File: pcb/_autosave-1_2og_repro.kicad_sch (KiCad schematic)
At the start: 217 parts, among them J1 Pico EzMate, J2 USB_B_Mini, J3 Raw Header, J4 JST PH S3B, J5 Foam, SW1 MX_SW_solder, SW10 MX_SW_solder, SW11 MX_SW_solder, SW12 MX_SW_solder, SW13 MX_SW_solder, SW14 MX_SW_solder, SW15 MX_SW_solder, SW16 MX_SW_solder, SW17 MX_SW_solder, SW18 MX_SW_solder, SW19 MX_SW_solder, SW2 MX_SW_solder, SW20 MX_SW_solder, SW21 MX_SW_solder, SW22 MX_SW_solder, SW23 MX_SW_solder, SW24 MX_SW_solder, SW25 MX_SW_solder, SW26 MX_SW_solder, SW27 MX_SW_solder, SW28 MX_SW_solder, SW29 MX_SW_solder, SW3 MX_SW_solder, SW30 MX_SW_solder, SW31 MX_SW_solder, SW32 MX_SW_solder, SW33 MX_SW_solder, SW34 MX_SW_solder, SW35 MX_SW_solder, SW36 MX_SW_solder, SW37 MX_SW_solder, SW38 MX_SW_solder, SW39 MX_SW_solder, SW4 MX_SW_solder, SW40 MX_SW_solder, SW41 MX_SW_solder, SW42 MX_SW_solder, SW43 MX_SW_solder, SW44 MX_SW_solder, SW45 MX_SW_solder, SW46 MX_SW_solder, SW47 MX_SW_solder, SW48 MX_SW_solder, SW49 MX_SW_solder, SW5 MX_SW_solder, SW50 MX_SW_solder, SW51 MX_SW_solder, SW52 MX_SW_solder, SW53 MX_SW_solder, SW54 MX_SW_solder, SW55 MX_SW_solder, SW56 MX_SW_solder, SW57 MX_SW_solder, SW58 MX_SW_solder, SW59 MX_SW_solder, SW6 MX_SW_solder, SW60 MX_SW_solder, SW61 MX_SW_solder, SW62 MX_SW_solder, SW63 MX_SW_solder, SW64 MX_SW_solder, SW65 MX_SW_solder, SW66 MX_SW_solder, SW67 MX_SW_solder, SW68 MX_SW_solder, SW69 MX_SW_solder, SW7 MX_SW_solder, SW70 MX_SW_solder, SW71 MX_SW_solder, SW72 MX_SW_solder, SW73 MX_SW_solder, SW74 MX_SW_solder, SW75 MX_SW_solder, SW76 MX_SW_solder, SW77 MX_SW_solder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

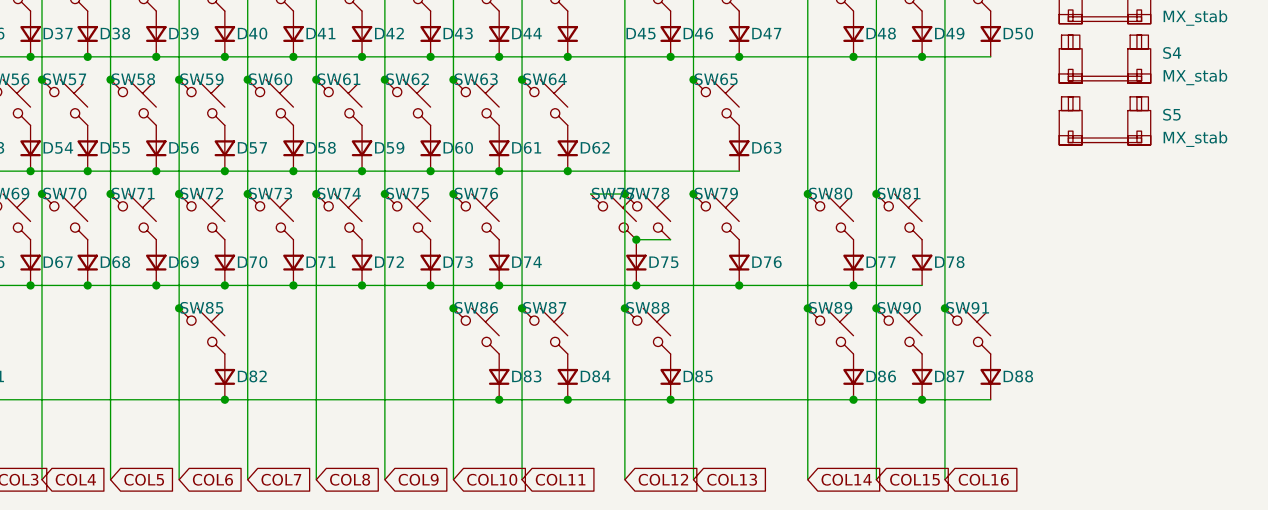
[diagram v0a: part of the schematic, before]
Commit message: add 6u support (firmware does not reflect this yet), usb 0548190519
previous USB is annoying to hand-solder without wick, using through-hole
pins may be less of a pain. 6u support is added because I miss my HHKB.
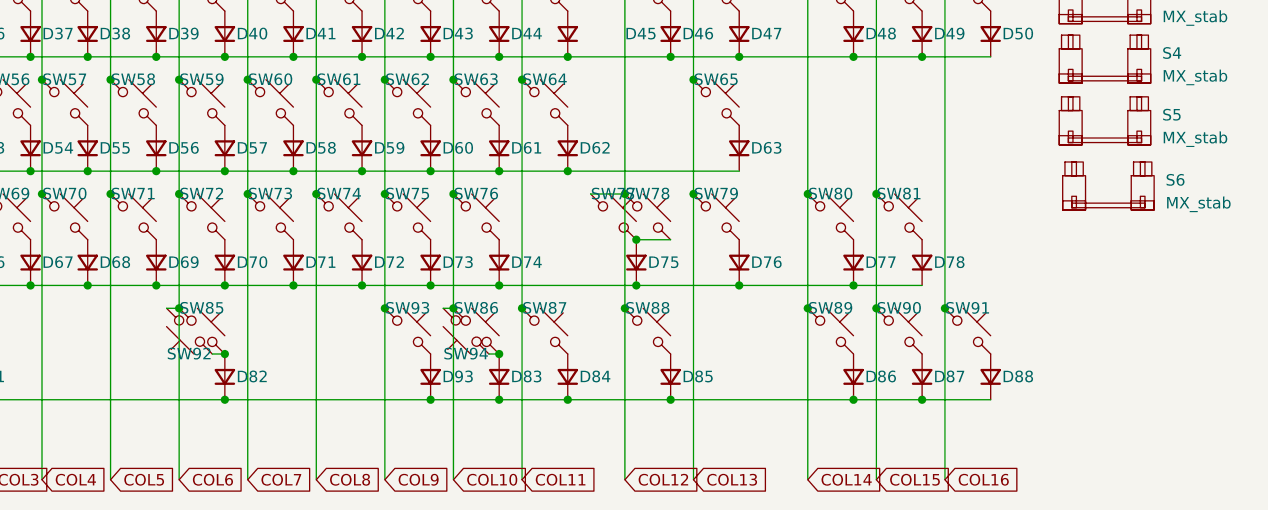
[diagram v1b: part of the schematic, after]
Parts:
- added D93: D_Small, Diode_SMD:D_SOD-123, symbol Device:D_Small
- added S6: MX_stab, marbastlib-mx:STAB_MX_6u, symbol marbastlib-mx:MX_stab
- added SW92, SW94: MX_SW_solder, marbastlib-mx:SW_MX_1u, symbol marbastlib-mx:MX_SW_solder
- added SW93: MX_SW_solder, marbastlib-mx:SW_MX_1.5u, symbol marbastlib-mx:MX_SW_solder
- J2: footprint random-keyboard-parts:Molex-0548190589 -> random-keyboard-parts:Molex-0548190519
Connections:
- net COL10: now also SW94.2
- net COL6: now also SW92.2
- net COL9: now also SW93.1
- net ROW5: now also D93.1 (K)
- net at D82.2 (A), SW85.2: now also SW92.1
- net at D83.2 (A), SW86.2: now also SW94.1
- new net: D93.2 (A), SW93.2
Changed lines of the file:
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@@
   (junction (at 226.06 119.253) (diameter 0) (color 0 0 0 0)
   )
+  (junction (at 191.77 144.653) (diameter 0) (color 0 0 0 0)
+  )
   (junction (at 137.16 154.813) (diameter 0) (color 0 0 0 0)
   )
+  (junction (at 173.99 149.733) (diameter 0) (color 0 0 0 0)
+  )
   (junction (at 139.7 106.553) (diameter 0) (color 0 0 0 0)
   )
@@
   (junction (at 129.54 116.713) (diameter 0) (color 0 0 0 0)
   )
+  (junction (at 204.47 149.733) (diameter 0) (color 0 0 0 0)
+  )
   (junction (at 176.53 106.553) (diameter 0) (color 0 0 0 0)
   )
@@
   (junction (at 133.985 50.165) (diameter 0) (color 0 0 0 0)
   )
+  (junction (at 196.85 154.813) (diameter 0) (color 0 0 0 0)
+  )
   (junction (at 231.14 142.113) (diameter 0) (color 0 0 0 0)
   )
@@
     (stroke (width 0) (type default))
   )
+  (wire (pts (xy 203.327 149.733) (xy 204.47 149.733))
+    (stroke (width 0) (type default))
+  )
   (wire (pts (xy 173.99 104.013) (xy 181.61 104.013))
     (stroke (width 0) (type default))
@@
     (stroke (width 0) (type default))
   )
+  (wire (pts (xy 167.513 144.653) (xy 168.91 144.653))
+    (stroke (width 0) (type default))
+  )
   (polyline (pts (xy 156.845 12.065) (xy 156.845 29.845))
     (stroke (width 0) (type default))
@@
     (stroke (width 0) (type default))
   )
-  (wire (pts (xy 204.47 154.813) (xy 173.99 154.813))
+  (wire (pts (xy 204.47 154.813) (xy 196.85 154.813))
     (stroke (width 0) (type default))
   )
@@
     (stroke (width 0) (type default))
   )
+  (wire (pts (xy 191.77 144.653) (xy 191.77 163.703))
+    (stroke (width 0) (type default))
+  )
   (wire (pts (xy 124.46 131.953) (xy 124.46 144.653))
     (stroke (width 0) (type default))
   )
-  (wire (pts (xy 191.77 131.953) (xy 191.77 163.703))
+  (wire (pts (xy 191.77 131.953) (xy 191.77 144.653))
     (stroke (width 0) (type default))
   )
@@
     (stroke (width 0) (type default))
   )
+  (wire (pts (xy 196.85 154.813) (xy 173.99 154.813))
+    (stroke (width 0) (type default))
+  )
   (wire (pts (xy 100.965 23.495) (xy 106.045 23.495))
     (stroke (width 0) (type default))
@@
     (stroke (width 0) (type default))
   )
+  (wire (pts (xy 198.247 144.653) (xy 199.39 144.653))
+    (stroke (width 0) (type default))
+  )
   (wire (pts (xy 196.85 104.013) (xy 204.47 104.013))
     (stroke (width 0) (type default))
@@
     (stroke (width 0) (type default))
   )
+  (wire (pts (xy 172.593 149.733) (xy 173.99 149.733))
+    (stroke (width 0) (type default))
+  )
   (wire (pts (xy 147.32 119.253) (xy 147.32 131.953))
     (stroke (width 0) (type default))
@@
     )
   )
+  (symbol (lib_id "marbastlib-mx:MX_SW_solder") (at 200.787 147.193 180) (unit 1)
+    (in_bom yes) (on_board yes) (dnp no)
+    (property "Reference" "SW94" (at 200.787 149.733 0)
+      (effects (font (size 1.27 1.27)))
+    )
+    (property "Value" "MX_SW_solder" (at 200.787 151.003 0)
+      (effects (font (size 1.27 1.27)) hide)
+    )
+    (property "Footprint" "marbastlib-mx:SW_MX_1u" (at 200.787 147.193 0)
+      (effects (font (size 1.27 1.27)) hide)
+    )
+    (property "Datasheet" "~" (at 200.787 147.193 0)
+      (effects (font (size 1.27 1.27)) hide)
+    )
+    (pin "1")
+    (pin "2")
+    (instances
+      (project "1_2og_repro"
+        (path "/70139223-fff4-476d-a728-a7aa752fc36c"
+          (reference "SW94") (unit 1)
+        )
+      )
+      (project "1_2_frl"
+        (path "/a8274e21-5f6e-4c7e-bbe0-133d7f65afea"
+          (reference "SW66") (unit 1)
+        )
+      )
+    )
+  )
   (symbol (lib_id "Device:D_Small") (at 137.16 101.473 90) (unit 1)
     (in_bom yes) (on_board yes) (dnp no)
@@
     )
   )
+  (symbol (lib_id "marbastlib-mx:MX_SW_solder") (at 170.053 147.193 180) (unit 1)
+    (in_bom yes) (on_board yes) (dnp no)
+    (property "Reference" "SW92" (at 170.053 149.733 0)
+      (effects (font (size 1.27 1.27)))
+    )
+    (property "Value" "MX_SW_solder" (at 170.053 151.003 0)
+      (effects (font (size 1.27 1.27)) hide)
+    )
+    (property "Footprint" "marbastlib-mx:SW_MX_1u" (at 170.053 147.193 0)
+      (effects (font (size 1.27 1.27)) hide)
+    )
+    (property "Datasheet" "~" (at 170.053 147.193 0)
+      (effects (font (size 1.27 1.27)) hide)
+    )
+    (pin "1")
+    (pin "2")
+    (instances
+      (project "1_2og_repro"
+        (path "/70139223-fff4-476d-a728-a7aa752fc36c"
+          (reference "SW92") (unit 1)
+        )
+      )
+      (project "1_2_frl"
+        (path "/a8274e21-5f6e-4c7e-bbe0-133d7f65afea"
+          (reference "SW65") (unit 1)
+        )
+      )
+    )
+  )
   (symbol (lib_id "power:VBUS") (at 178.435 17.653 0) (unit 1)
     (in_bom yes) (on_board yes) (dnp no) (fields_autoplaced)
@@
     )
   )
+  (symbol (lib_id "Device:D_Small") (at 196.85 152.273 90) (unit 1)
+    (in_bom yes) (on_board yes) (dnp no)
+    (property "Reference" "D93" (at 198.12 152.273 90)
+      (effects (font (size 1.27 1.27)) (justify right))
+    )
+    (property "Value" "D_Small" (at 199.39 154.178 90)
+      (effects (font (size 1.27 1.27)) (justify right) hide)
+    )
+    (property "Footprint" "Diode_SMD:D_SOD-123" (at 196.85 152.273 90)
+      (effects (font (size 1.27 1.27)) hide)
+    )
+    (property "Datasheet" "~" (at 196.85 152.273 90)
+      (effects (font (size 1.27 1.27)) hide)
+    )
+    (property "Sim.Device" "D" (at 196.85 152.273 0)
+      (effects (font (size 1.27 1.27)) hide)
+    )
+    (property "Sim.Pins" "1=K 2=A" (at 196.85 152.273 0)
+      (effects (font (size 1.27 1.27)) hide)
+    )
+    (pin "1")
+    (pin "2")
+    (instances
+      (project "1_2og_repro"
+        (path "/70139223-fff4-476d-a728-a7aa752fc36c"
+          (reference "D93") (unit 1)
+        )
+      )
+      (project "1_2_frl"
+        (path "/a8274e21-5f6e-4c7e-bbe0-133d7f65afea"
+          (reference "D57") (unit 1)
+        )
+      )
+    )
+  )
   (symbol (lib_id "Mechanical:MountingHole_Pad") (at 164.973 63.627 180) (unit 1)
     (in_bom yes) (on_board yes) (dnp no) (fields_autoplaced)
@@
       (effects (font (size 1.27 1.27)))
     )
-    (property "Footprint" "random-keyboard-parts:Molex-0548190589" (at 81.026 44.577 0)
+    (property "Footprint" "random-keyboard-parts:Molex-0548190519" (at 81.026 44.577 0)
       (effects (font (size 1.524 1.524)) hide)
     )
@@
     )
   )
+  (symbol (lib_id "marbastlib-mx:MX_SW_solder") (at 194.31 147.193 0) (unit 1)
+    (in_bom yes) (on_board yes) (dnp no)
+    (property "Reference" "SW93" (at 194.31 144.653 0)
+      (effects (font (size 1.27 1.27)))
+    )
+    (property "Value" "MX_SW_solder" (at 194.31 143.383 0)
+      (effects (font (size 1.27 1.27)) hide)
+    )
+    (property "Footprint" "marbastlib-mx:SW_MX_1.5u" (at 194.31 147.193 0)
+      (effects (font (size 1.27 1.27)) hide)
+    )
+    (property "Datasheet" "~" (at 194.31 147.193 0)
+      (effects (font (size 1.27 1.27)) hide)
+    )
+    (pin "1")
+    (pin "2")
+    (instances
+      (project "1_2og_repro"
+        (path "/70139223-fff4-476d-a728-a7aa752fc36c"
+          (reference "SW93") (unit 1)
+        )
+      )
+      (project "1_2_frl"
+        (path "/a8274e21-5f6e-4c7e-bbe0-133d7f65afea"
+          (reference "SW65") (unit 1)
+        )
+      )
+    )
+  )
   (symbol (lib_id "Device:C_Small") (at 141.605 20.955 0) (unit 1)
     (in_bom yes) (on_board yes) (dnp no) (fields_autoplaced)
@@
         )
       )
+    )
+  )
+  (symbol (lib_id "marbastlib-mx:MX_stab") (at 272.161 131.191 0) (unit 1)
+    (in_bom yes) (on_board yes) (dnp no) (fields_autoplaced)
+    (property "Reference" "S6" (at 278.511 130.429 0)
+      (effects (font (size 1.27 1.27)) (justify left))
+    )
+    (property "Value" "MX_stab" (at 278.511 132.969 0)
+      (effects (font (size 1.27 1.27)) (justify left))
+    )
+    (property "Footprint" "marbastlib-mx:STAB_MX_6u" (at 272.161 131.191 0)
+      (effects (font (size 1.27 1.27)) hide)
+    )
+    (property "Datasheet" "" (at 272.161 131.191 0)
+      (effects (font (size 1.27 1.27)) hide)
+    )
+    (instances
+      (project "1_2og_repro"
+        (path "/70139223-fff4-476d-a728-a7aa752fc36c"
+          (reference "S6") (unit 1)
+        )
+      )
